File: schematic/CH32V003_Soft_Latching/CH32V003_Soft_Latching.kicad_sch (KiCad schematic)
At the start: 9 parts, among them Q1 PMOS, Q2 NMOS, SW1 SW_Push, U1 CH32V003J4M6

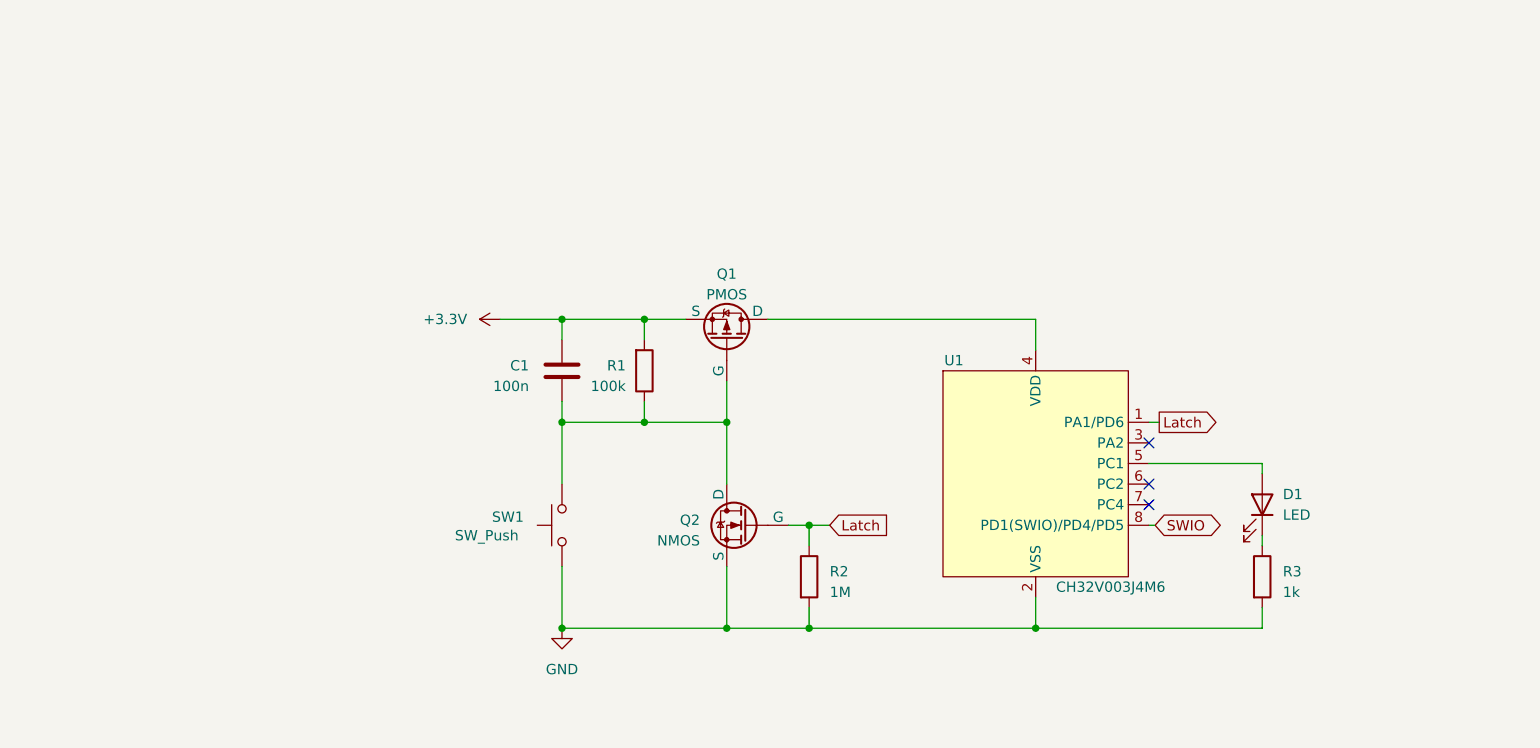
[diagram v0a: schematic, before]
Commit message: Update schematic to latch and input
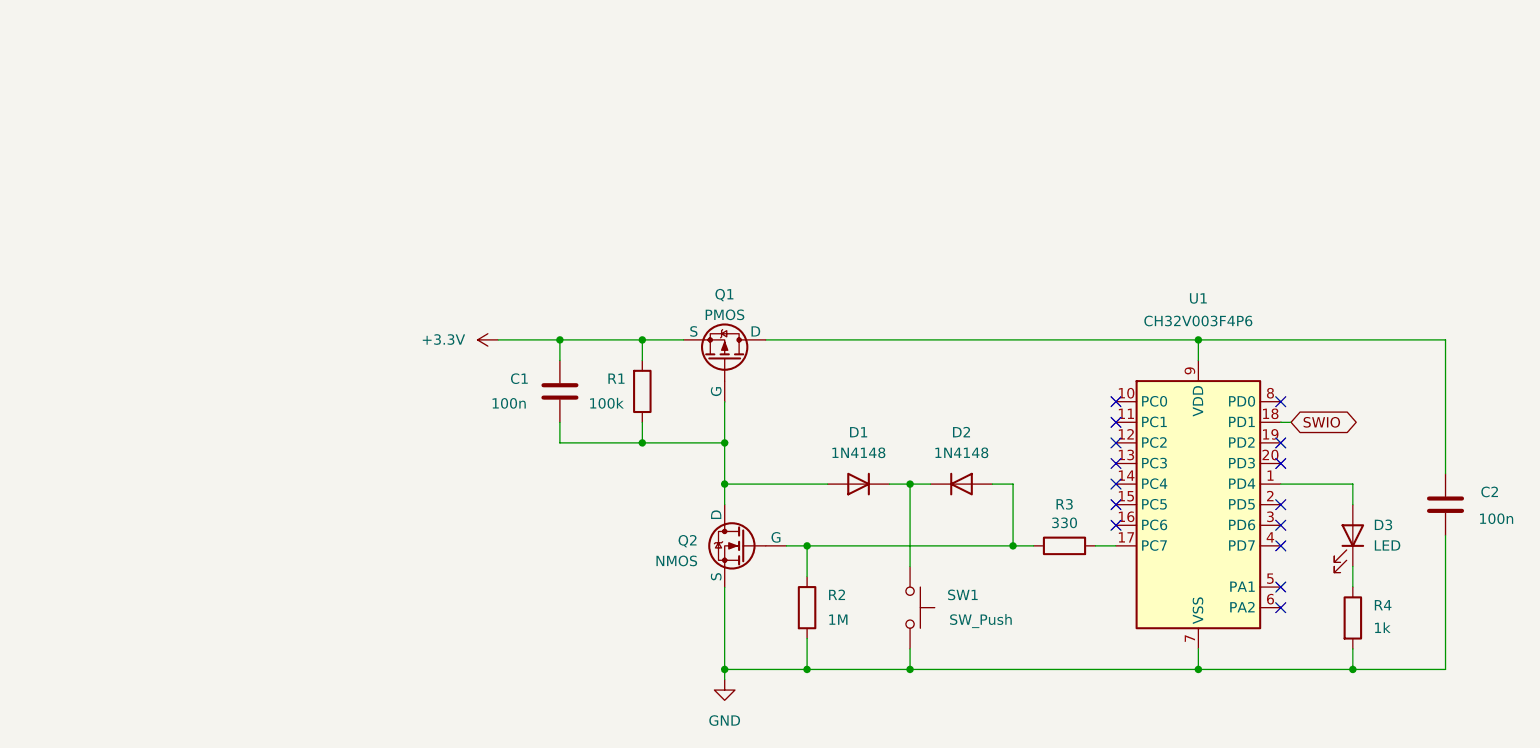
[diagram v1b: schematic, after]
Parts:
- removed U1: CH32V003J4M6, Package_SO:SSOP-8_3.9x5.05mm_P1.27mm, symbol CH32V003J4M6:CH32V003J4M6
- added C2: 100n, symbol Device:C
- added D1, D2: 1N4148, Diode_THT:D_DO-35_SOD27_P7.62mm_Horizontal, symbol Diode:1N4148
- added R3: 330, symbol Device:R
- added U1: CH32V003F4P6, Package_SO:TSSOP-20_4.4x6.5mm_P0.65mm, symbol MCU_WCH_CH32V0:CH32V003FxPx
- renumbered D1 to D3, R3 to R4
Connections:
- net GND: now also C2.2, U1.7 (VSS)
- net SWIO: now also U1.18 (PD1)
- net at C1.2, Q1.2 (G), Q2.1 (D)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: now also D1.2 (A); no longer SW1.2
- net at Q1.1 (D): now also C2.1, U1.9 (VDD)
- net at D3.2 (A): now also U1.1 (PD4)
- net Latch: no longer names the net of Q2.2 (G), R2.1
- net Latch: now also D2.2 (A), R3.1
- new net: R3.2, U1.17 (PC7)
- new net: D1.1 (K), D2.1 (K), SW1.2
- no-connect marks 3 -> 15
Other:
- moved on the sheet: C1, D3, Q1, Q2, R1, R2, R4, SW1

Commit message: Update schematic
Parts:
- renumbered R4 to R_led
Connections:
- net at U1.1 (PD4): no longer D3.2 (A)
- net at U1.2 (PD5): now also D3.2 (A)
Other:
- moved on the sheet: C1, C2, D1, D2, D3, Q1, Q2, R1, R2, R3, R_led, SW1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
